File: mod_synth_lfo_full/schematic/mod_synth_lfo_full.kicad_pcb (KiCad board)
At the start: 2 copper layers, 62.2 x 109.2 mm, 75 parts, among them J1 CV, J2 Conn_02x08_Odd_Even, J3 SIN, J4 COS, J5 TRI, J6 SQR, J7 RAMP UP, J8 RAMP DOWN, Q1 BC550, Q2 BC550, Q3 BC550, Q4 BC550, Q5 BC550, U1 TL072, U2 TL072, U3 TL072, U4 TL074

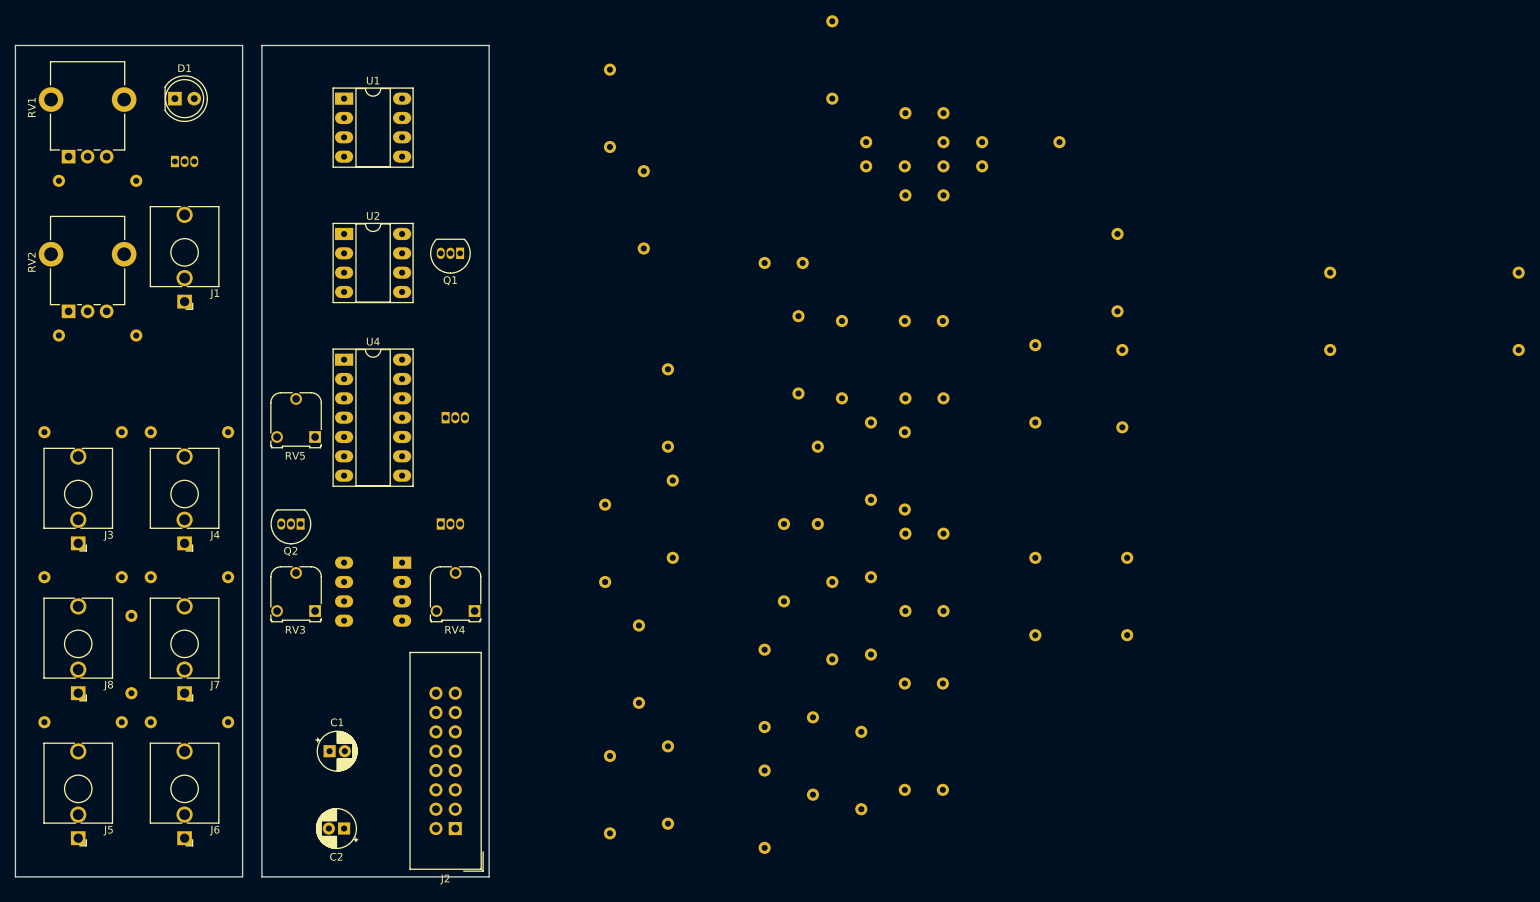
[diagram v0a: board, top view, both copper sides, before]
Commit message: Possible three PCB layout
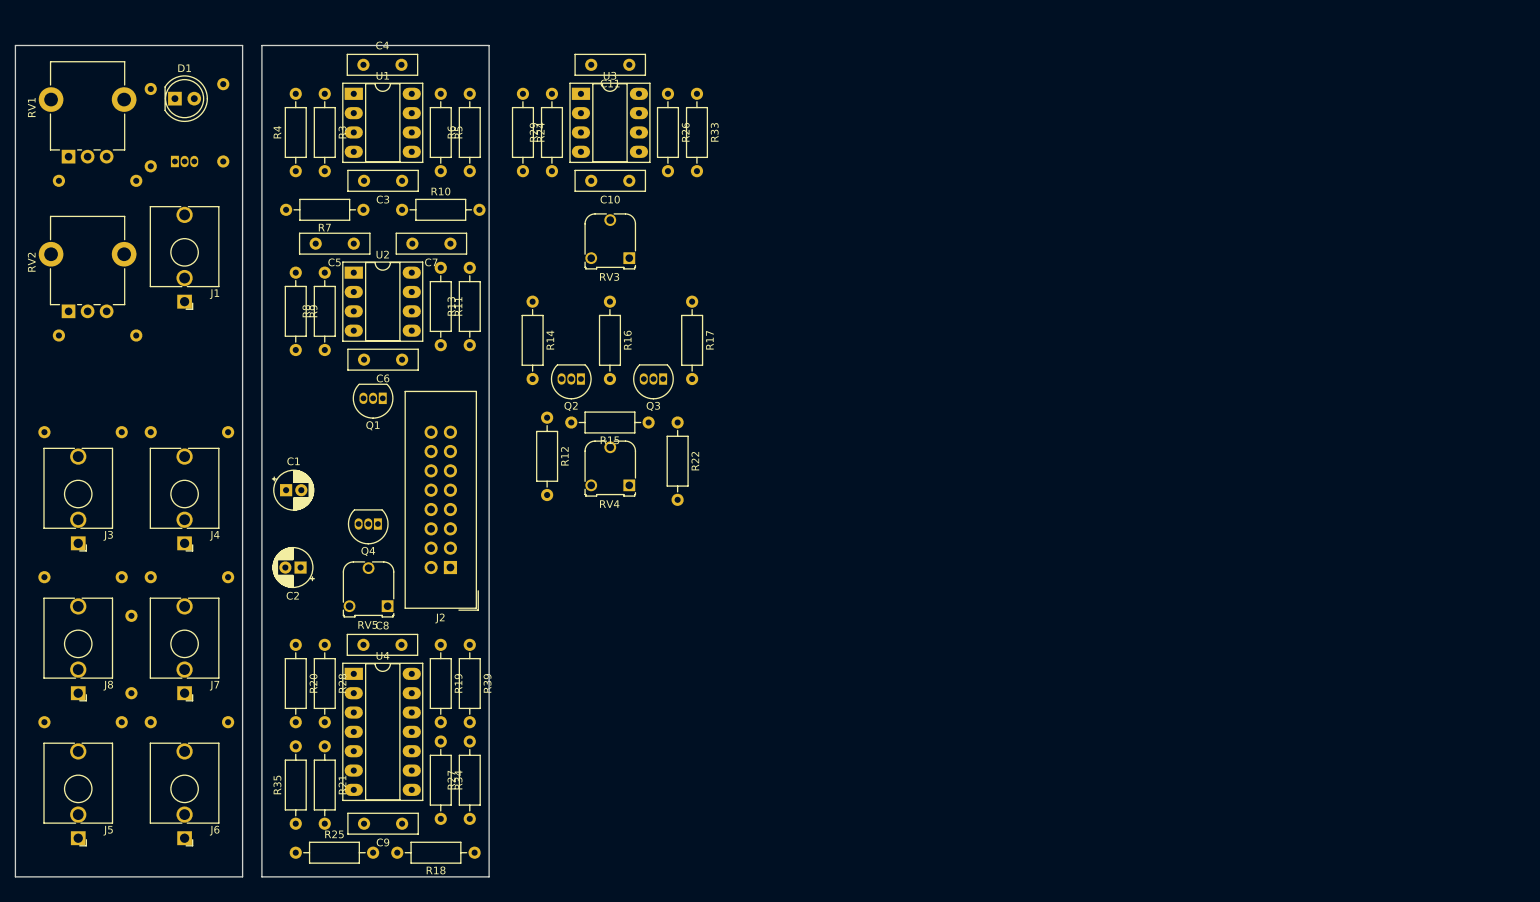
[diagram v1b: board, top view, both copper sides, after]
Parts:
- C10, C11, C3, C4, C5, C6, C7, C8, C9, Q3, Q4, R10, R11, R12, R13, R14, R15, R16, R17, R18, R19, R20, R21, R22, R24, R25, R26, R27, R28, R29, R3, R33, R34, R35, R39, R4, R5, R6, R7, R8, R9, U3: moved to F.Cu
- moved R22 110.9 mm to (157.5, 72.4), turned to 270 degrees
- moved C4 108.0 mm to (116.2, 25.4)
- moved R8 104.3 mm to (111.1, 62.9)
- moved C3 103.7 mm to (121.3, 40.6), turned to 180 degrees
- moved R10 98.8 mm to (121.3, 44.5), turned to 0 degrees
- moved R28 94.0 mm to (111.1, 101.6)
- moved C9 90.4 mm to (121.3, 125.1)
- moved R18 90.4 mm to (130.8, 128.9), turned to 180 degrees
- moved R4 90.2 mm to (107.3, 39.4), turned to 90 degrees
- moved R15 90.0 mm to (153.7, 72.4), turned to 180 degrees
- moved R38 90.0 mm to (88.3, 28.6)
- moved R3 86.6 mm to (111.1, 29.2), turned to 270 degrees
- moved C5 86.3 mm to (114.9, 48.9)
- moved C8 82.9 mm to (116.2, 101.6)
- moved R21 82.3 mm to (111.1, 114.9), turned to 270 degrees
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
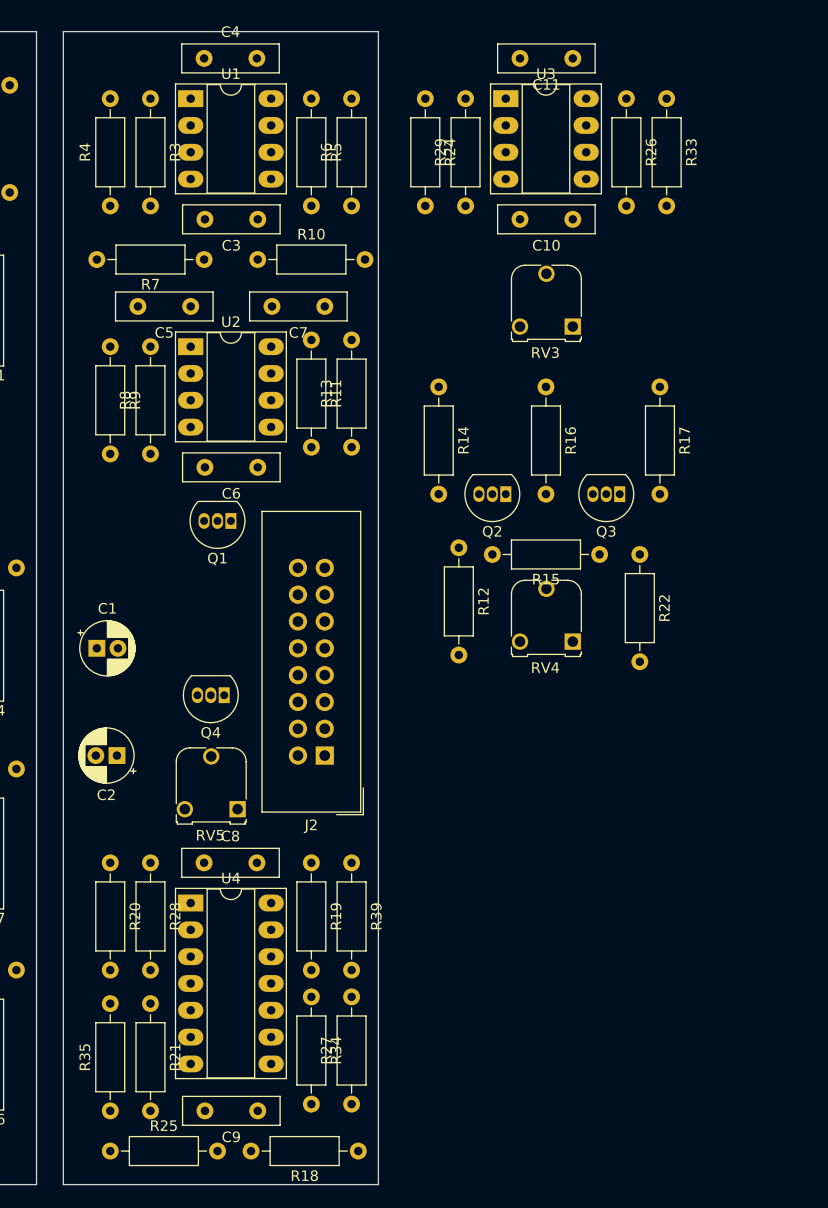
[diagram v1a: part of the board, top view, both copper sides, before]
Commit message: Alter PCB layouts
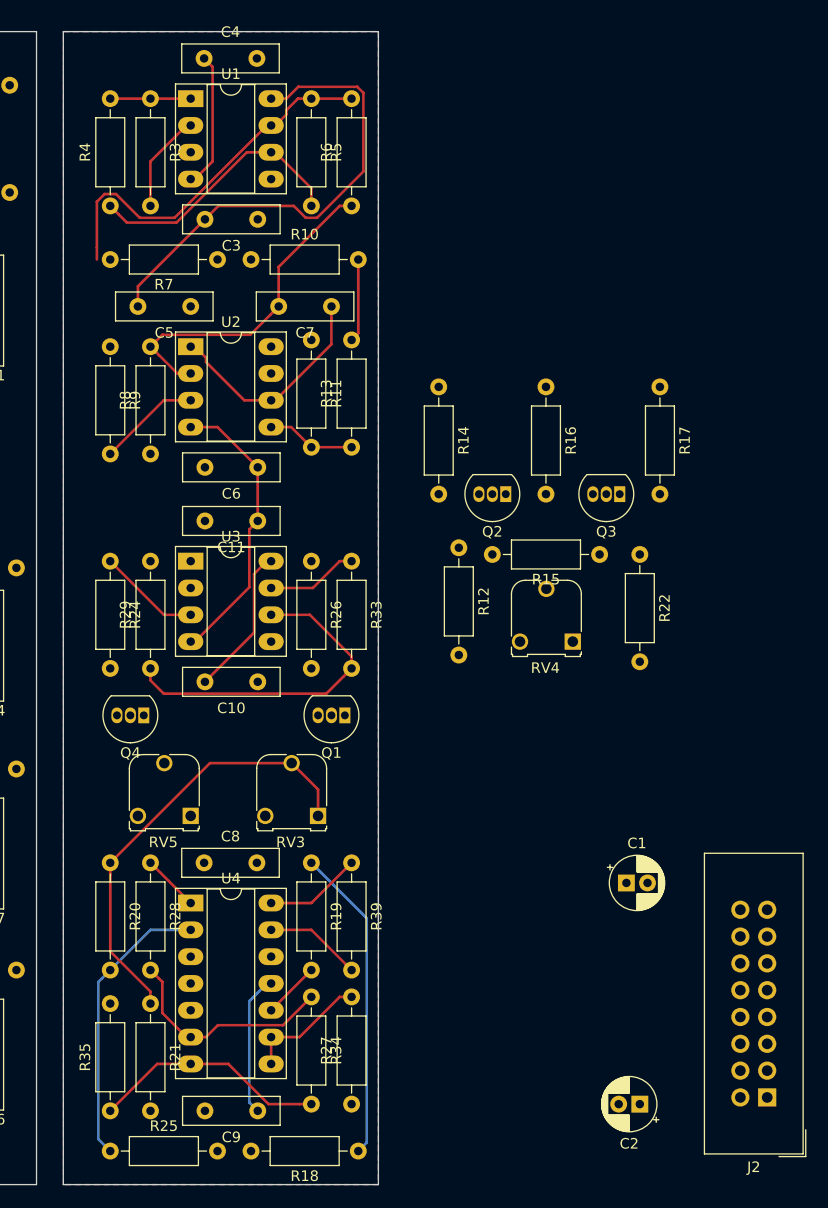
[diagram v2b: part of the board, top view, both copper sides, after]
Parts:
- moved C2 59.5 mm to (157.5, 124.5)
- moved C1 54.9 mm to (156.2, 103.5)
- moved R26 53.0 mm to (126.4, 73.0)
- moved C11 53.0 mm to (121.3, 69.2)
- moved R24 53.0 mm to (107.3, 73.0)
- moved R29 53.0 mm to (111.1, 83.2)
- moved R33 53.0 mm to (130.2, 73.0)
- moved U3 53.0 mm to (114.9, 73.0)
- moved C10 53.0 mm to (121.3, 84.5)
- moved J2 53.0 mm to (169.5, 123.8)
- moved RV3 52.3 mm to (127.0, 97.2)
- moved Q1 21.3 mm to (129.5, 87.6)
- moved Q4 7.85 mm to (110.5, 87.6)
- moved RV5 4.49 mm to (114.9, 97.2)
- moved R7 1.27 mm to (117.5, 44.5)
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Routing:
- net Net-(C7-Pad1): track 0.00 -> 63.5 mm
- net +12V: track 0.00 -> 59.9 mm
- net -12V: track 0.00 -> 53.6 mm
- net Net-(R10-Pad2): track 0.00 -> 37.7 mm
- net Net-(R5-Pad1): track 0.00 -> 35.7 mm
- net Net-(R29-Pad1): track 0.00 -> 32.1 mm
- net Net-(C7-Pad2): track 0.00 -> 31.6 mm
- net Net-(R20-Pad2): track 0.00 -> 27.3 mm
- net Net-(R4-Pad1): track 0.00 -> 25.5 mm
- net Net-(R34-Pad2): track 0.00 -> 22.5 mm
- net Net-(R28-Pad2): track 0.00 -> 21.2 mm
- net Net-(R27-Pad2): track 0.00 -> 11.7 mm
- net Net-(R7-Pad1): track 0.00 -> 9.72 mm
- net Net-(Q3-Pad1): track 0.00 -> 9.72 mm
- net Net-(R1-Pad1): track 0.00 -> 9.43 mm
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- added copper zone on B.Cu, net GND
- added copper zone on F.Cu, net GND
